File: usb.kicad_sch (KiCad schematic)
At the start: 10 parts, among them J7 USB_C_Receptacle_USB2.0, U28 USBLC6-4SC6

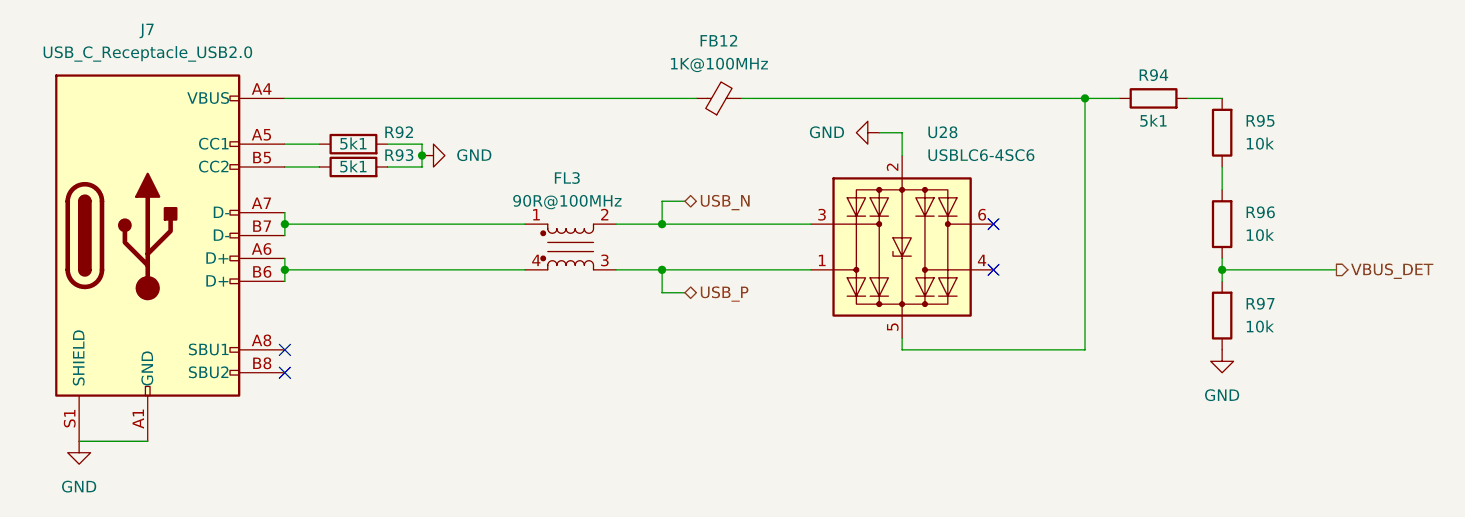
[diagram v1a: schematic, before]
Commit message: pcb: Finish Layout for rev0_3 - Assign MFR_PN for all Components - schematics changes:   - drivestage: Add Switch to optionally enable Modulation Signal Termination   -             Add alternate Precision Power Resistor   -             Modify the RC network values at TIA LPF Output   - MCU: Add Redundant 2.54mm pitch Programming Header   - thermostat: Duplicate the power filter network for alternate Temperature ADC
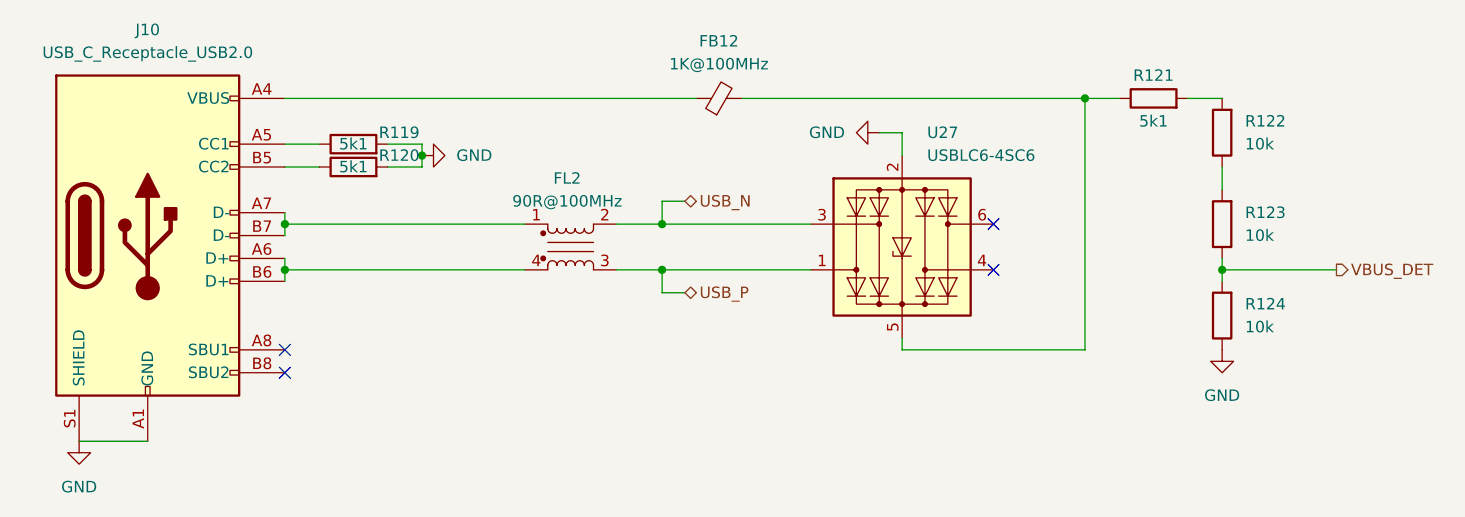
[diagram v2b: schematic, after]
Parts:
- renumbered FL3 to FL2, J7 to J10, R92 to R119, R93 to R120, R94 to R121, R95 to R122, R96 to R123, R97 to R124, U28 to U27
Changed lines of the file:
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@@
     (title "Kirdy")
     (date "2022-07-03")
-    (rev "r0.1")
+    (rev "r0.3")
     (company "M-Labs")
-    (comment 1 "Alex Wong Tat Hang")
+    (comment 1 "Linus Woo Chun Kit")
   )
   (junction (at 143.51 101.6) (diameter 0) (color 0 0 0 0)
@@
   (symbol (lib_id "power:GND") (at 247.65 115.57 0) (unit 1)
     (in_bom yes) (on_board yes) (dnp no) (fields_autoplaced)
-    (property "Reference" "#PWR0155" (at 247.65 121.92 0)
+    (property "Reference" "#PWR0184" (at 247.65 121.92 0)
       (effects (font (size 1.27 1.27)) hide)
     )
@@
       (project "kirdy"
         (path "/88da1dd8-9274-4b55-84fb-90006c9b6e8f/70187dee-b8b1-417f-999f-47b1dfda0f58"
-          (reference "#PWR0155") (unit 1)
+          (reference "#PWR0184") (unit 1)
         )
       )
@@
   (symbol (lib_id "power:GND") (at 158.75 93.98 90) (unit 1)
     (in_bom yes) (on_board yes) (dnp no) (fields_autoplaced)
-    (property "Reference" "#PWR0153" (at 165.1 93.98 0)
+    (property "Reference" "#PWR0182" (at 165.1 93.98 0)
       (effects (font (size 1.27 1.27)) hide)
     )
@@
       (project "kirdy"
         (path "/88da1dd8-9274-4b55-84fb-90006c9b6e8f/70187dee-b8b1-417f-999f-47b1dfda0f58"
-          (reference "#PWR0153") (unit 1)
+          (reference "#PWR0182") (unit 1)
         )
       )
@@
   (symbol (lib_id "power:GND") (at 209.55 91.44 270) (unit 1)
     (in_bom yes) (on_board yes) (dnp no) (fields_autoplaced)
-    (property "Reference" "#PWR0154" (at 203.2 91.44 0)
+    (property "Reference" "#PWR0183" (at 203.2 91.44 0)
       (effects (font (size 1.27 1.27)) hide)
     )
@@
       (project "kirdy"
         (path "/88da1dd8-9274-4b55-84fb-90006c9b6e8f/70187dee-b8b1-417f-999f-47b1dfda0f58"
-          (reference "#PWR0154") (unit 1)
+          (reference "#PWR0183") (unit 1)
         )
       )
@@
   (symbol (lib_id "Connector:USB_C_Receptacle_USB2.0") (at 128.27 102.87 0) (unit 1)
     (in_bom yes) (on_board yes) (dnp no) (fields_autoplaced)
-    (property "Reference" "J7" (at 128.27 80.01 0)
+    (property "Reference" "J10" (at 128.27 80.01 0)
       (effects (font (size 1.27 1.27)))
     )
@@
       (project "kirdy"
         (path "/88da1dd8-9274-4b55-84fb-90006c9b6e8f/70187dee-b8b1-417f-999f-47b1dfda0f58"
-          (reference "J7") (unit 1)
+          (reference "J10") (unit 1)
         )
       )
@@
   (symbol (lib_id "Device:R") (at 151.13 92.71 90) (unit 1)
     (in_bom yes) (on_board yes) (dnp no)
-    (property "Reference" "R92" (at 156.21 91.44 90)
+    (property "Reference" "R119" (at 156.21 91.44 90)
       (effects (font (size 1.27 1.27)))
     )
@@
       (project "kirdy"
         (path "/88da1dd8-9274-4b55-84fb-90006c9b6e8f/70187dee-b8b1-417f-999f-47b1dfda0f58"
-          (reference "R92") (unit 1)
+          (reference "R119") (unit 1)
         )
       )
@@
   (symbol (lib_id "Device:R") (at 247.65 111.76 180) (unit 1)
     (in_bom yes) (on_board yes) (dnp no) (fields_autoplaced)
-    (property "Reference" "R97" (at 250.19 110.4899 0)
+    (property "Reference" "R124" (at 250.19 110.4899 0)
       (effects (font (size 1.27 1.27)) (justify right))
     )
@@
       (project "kirdy"
         (path "/88da1dd8-9274-4b55-84fb-90006c9b6e8f/70187dee-b8b1-417f-999f-47b1dfda0f58"
-          (reference "R97") (unit 1)
+          (reference "R124") (unit 1)
         )
       )
@@
   (symbol (lib_id "Power_Protection:USBLC6-4SC6") (at 212.09 104.14 0) (mirror x) (unit 1)
     (in_bom yes) (on_board yes) (dnp no) (fields_autoplaced)
-    (property "Reference" "U28" (at 214.8587 91.44 0)
+    (property "Reference" "U27" (at 214.8587 91.44 0)
       (effects (font (size 1.27 1.27)) (justify left))
     )
@@
       (project "kirdy"
         (path "/88da1dd8-9274-4b55-84fb-90006c9b6e8f/70187dee-b8b1-417f-999f-47b1dfda0f58"
-          (reference "U28") (unit 1)
+          (reference "U27") (unit 1)
         )
       )
@@
   (symbol (lib_id "Device:R") (at 151.13 95.25 90) (unit 1)
     (in_bom yes) (on_board yes) (dnp no)
-    (property "Reference" "R93" (at 156.21 93.98 90)
+    (property "Reference" "R120" (at 156.21 93.98 90)
       (effects (font (size 1.27 1.27)))
     )
@@
       (project "kirdy"
         (path "/88da1dd8-9274-4b55-84fb-90006c9b6e8f/70187dee-b8b1-417f-999f-47b1dfda0f58"
-          (reference "R93") (unit 1)
+          (reference "R120") (unit 1)
         )
       )
@@
   (symbol (lib_id "Device:R") (at 240.03 87.63 90) (unit 1)
     (in_bom yes) (on_board yes) (dnp no)
-    (property "Reference" "R94" (at 240.03 85.09 90)
+    (property "Reference" "R121" (at 240.03 85.09 90)
       (effects (font (size 1.27 1.27)))
     )
@@
       (project "kirdy"
         (path "/88da1dd8-9274-4b55-84fb-90006c9b6e8f/70187dee-b8b1-417f-999f-47b1dfda0f58"
-          (reference "R94") (unit 1)
+          (reference "R121") (unit 1)
         )
       )
@@
   (symbol (lib_id "Device:R") (at 247.65 101.6 180) (unit 1)
     (in_bom yes) (on_board yes) (dnp no) (fields_autoplaced)
-    (property "Reference" "R96" (at 250.19 100.3299 0)
+    (property "Reference" "R123" (at 250.19 100.3299 0)
       (effects (font (size 1.27 1.27)) (justify right))
     )
@@
       (project "kirdy"
         (path "/88da1dd8-9274-4b55-84fb-90006c9b6e8f/70187dee-b8b1-417f-999f-47b1dfda0f58"
-          (reference "R96") (unit 1)
+          (reference "R123") (unit 1)
         )
       )
@@
   (symbol (lib_id "Device:R") (at 247.65 91.44 180) (unit 1)
     (in_bom yes) (on_board yes) (dnp no) (fields_autoplaced)
-    (property "Reference" "R95" (at 250.19 90.1699 0)
+    (property "Reference" "R122" (at 250.19 90.1699 0)
       (effects (font (size 1.27 1.27)) (justify right))
     )
@@
       (project "kirdy"
         (path "/88da1dd8-9274-4b55-84fb-90006c9b6e8f/70187dee-b8b1-417f-999f-47b1dfda0f58"
-          (reference "R95") (unit 1)
+          (reference "R122") (unit 1)
         )
       )
@@
   (symbol (lib_id "kirdy:Filter_EMI_LL_1423") (at 175.26 104.14 0) (unit 1)
     (in_bom yes) (on_board yes) (dnp no)
-    (property "Reference" "FL3" (at 174.879 96.52 0)
+    (property "Reference" "FL2" (at 174.879 96.52 0)
       (effects (font (size 1.27 1.27)))
     )
@@
       (project "kirdy"
         (path "/88da1dd8-9274-4b55-84fb-90006c9b6e8f/70187dee-b8b1-417f-999f-47b1dfda0f58"
-          (reference "FL3") (unit 1)
+          (reference "FL2") (unit 1)
         )
       )
@@
   (symbol (lib_id "power:GND") (at 120.65 125.73 0) (unit 1)
     (in_bom yes) (on_board yes) (dnp no) (fields_autoplaced)
-    (property "Reference" "#PWR0152" (at 120.65 132.08 0)
+    (property "Reference" "#PWR0181" (at 120.65 132.08 0)
       (effects (font (size 1.27 1.27)) hide)
     )
@@
       (project "kirdy"
         (path "/88da1dd8-9274-4b55-84fb-90006c9b6e8f/70187dee-b8b1-417f-999f-47b1dfda0f58"
-          (reference "#PWR0152") (unit 1)
-        )
-      )
+          (reference "#PWR0181") (unit 1)
+        )
+      )

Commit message: sch: Update Title Block Info - rev0.3 -> rev0_3 - Correct the title of each schematics - Update the modified time
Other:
- company: M-Labs -> M-Labs Limited
- title: Kirdy -> USB
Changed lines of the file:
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@@
   (paper "A3")
   (title_block
-    (title "Kirdy")
-    (date "2022-07-03")
-    (rev "r0.3")
-    (company "M-Labs")
+    (title "USB")
+    (date "2023-11-09")
+    (rev "r0_3")
+    (company "M-Labs Limited")
     (comment 1 "Linus Woo Chun Kit")
   )

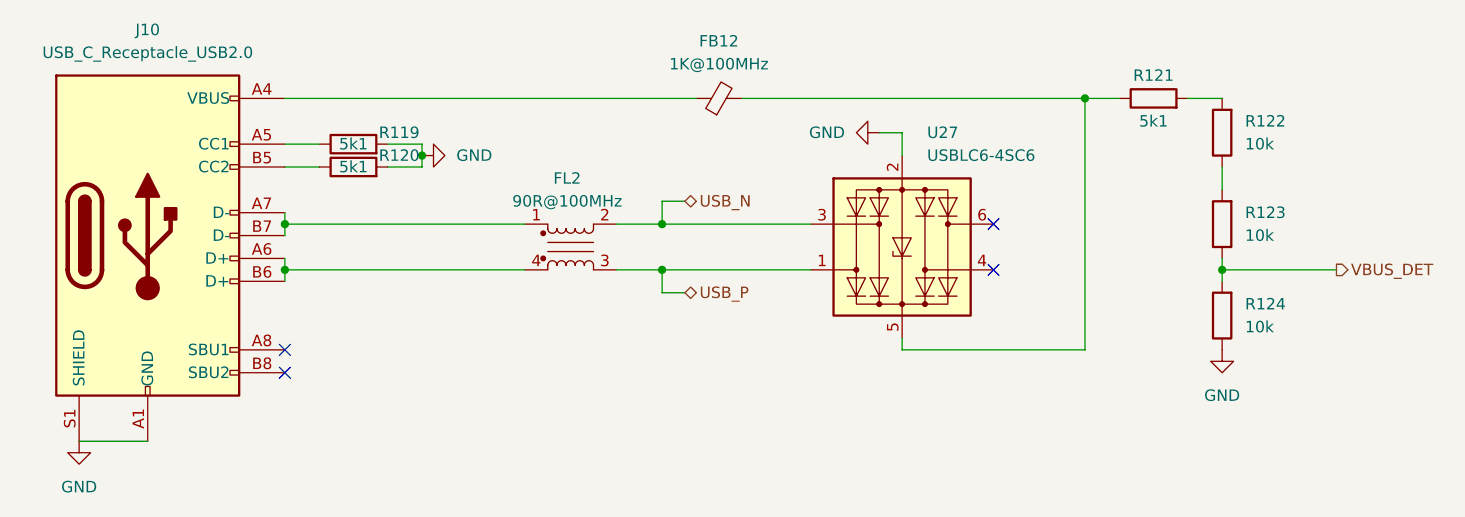
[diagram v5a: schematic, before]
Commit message: Reassign Reference Designators for all Symbols
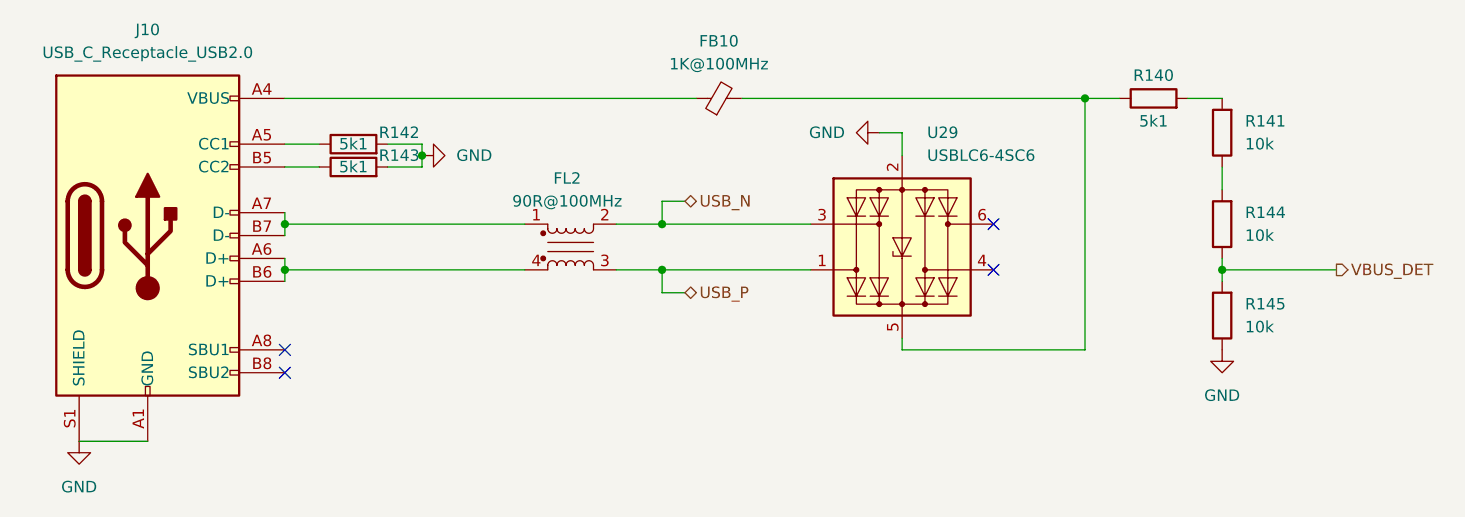
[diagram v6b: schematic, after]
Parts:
- renumbered FB12 to FB10, R121 to R140, R122 to R141, R119 to R142, R120 to R143, R123 to R144, R124 to R145, U27 to U29
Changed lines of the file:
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@@
   (symbol (lib_id "power:GND") (at 247.65 115.57 0) (unit 1)
     (in_bom yes) (on_board yes) (dnp no) (fields_autoplaced)
-    (property "Reference" "#PWR0185" (at 247.65 121.92 0)
+    (property "Reference" "#PWR0233" (at 247.65 121.92 0)
       (effects (font (size 1.27 1.27)) hide)
     )
@@
       (project "kirdy"
         (path "/88da1dd8-9274-4b55-84fb-90006c9b6e8f/70187dee-b8b1-417f-999f-47b1dfda0f58"
-          (reference "#PWR0185") (unit 1)
+          (reference "#PWR0233") (unit 1)
         )
       )
@@
   (symbol (lib_id "power:GND") (at 158.75 93.98 90) (unit 1)
     (in_bom yes) (on_board yes) (dnp no) (fields_autoplaced)
-    (property "Reference" "#PWR0183" (at 165.1 93.98 0)
+    (property "Reference" "#PWR0232" (at 165.1 93.98 0)
       (effects (font (size 1.27 1.27)) hide)
     )
@@
       (project "kirdy"
         (path "/88da1dd8-9274-4b55-84fb-90006c9b6e8f/70187dee-b8b1-417f-999f-47b1dfda0f58"
-          (reference "#PWR0183") (unit 1)
+          (reference "#PWR0232") (unit 1)
         )
       )
@@
   (symbol (lib_id "power:GND") (at 209.55 91.44 270) (unit 1)
     (in_bom yes) (on_board yes) (dnp no) (fields_autoplaced)
-    (property "Reference" "#PWR0184" (at 203.2 91.44 0)
+    (property "Reference" "#PWR0231" (at 203.2 91.44 0)
       (effects (font (size 1.27 1.27)) hide)
     )
@@
       (project "kirdy"
         (path "/88da1dd8-9274-4b55-84fb-90006c9b6e8f/70187dee-b8b1-417f-999f-47b1dfda0f58"
-          (reference "#PWR0184") (unit 1)
+          (reference "#PWR0231") (unit 1)
         )
       )
@@
   (symbol (lib_id "Device:R") (at 151.13 92.71 90) (unit 1)
     (in_bom yes) (on_board yes) (dnp no)
-    (property "Reference" "R119" (at 156.21 91.44 90)
+    (property "Reference" "R142" (at 156.21 91.44 90)
       (effects (font (size 1.27 1.27)))
     )
@@
       (project "kirdy"
         (path "/88da1dd8-9274-4b55-84fb-90006c9b6e8f/70187dee-b8b1-417f-999f-47b1dfda0f58"
-          (reference "R119") (unit 1)
+          (reference "R142") (unit 1)
         )
       )
@@
   (symbol (lib_id "Device:R") (at 247.65 111.76 180) (unit 1)
     (in_bom yes) (on_board yes) (dnp no) (fields_autoplaced)
-    (property "Reference" "R124" (at 250.19 110.4899 0)
+    (property "Reference" "R145" (at 250.19 110.4899 0)
       (effects (font (size 1.27 1.27)) (justify right))
     )
@@
       (project "kirdy"
         (path "/88da1dd8-9274-4b55-84fb-90006c9b6e8f/70187dee-b8b1-417f-999f-47b1dfda0f58"
-          (reference "R124") (unit 1)
+          (reference "R145") (unit 1)
         )
       )
@@
   (symbol (lib_id "Power_Protection:USBLC6-4SC6") (at 212.09 104.14 0) (mirror x) (unit 1)
     (in_bom yes) (on_board yes) (dnp no) (fields_autoplaced)
-    (property "Reference" "U27" (at 214.8587 91.44 0)
+    (property "Reference" "U29" (at 214.8587 91.44 0)
       (effects (font (size 1.27 1.27)) (justify left))
     )
@@
       (project "kirdy"
         (path "/88da1dd8-9274-4b55-84fb-90006c9b6e8f/70187dee-b8b1-417f-999f-47b1dfda0f58"
-          (reference "U27") (unit 1)
+          (reference "U29") (unit 1)
         )
       )
@@
   (symbol (lib_id "Device:FerriteBead_Small") (at 191.77 87.63 90) (unit 1)
     (in_bom yes) (on_board yes) (dnp no) (fields_autoplaced)
-    (property "Reference" "FB12" (at 191.7319 81.28 90)
+    (property "Reference" "FB10" (at 191.7319 81.28 90)
       (effects (font (size 1.27 1.27)))
     )
@@
       (project "kirdy"
         (path "/88da1dd8-9274-4b55-84fb-90006c9b6e8f/70187dee-b8b1-417f-999f-47b1dfda0f58"
-          (reference "FB12") (unit 1)
+          (reference "FB10") (unit 1)
         )
       )
@@
   (symbol (lib_id "Device:R") (at 151.13 95.25 90) (unit 1)
     (in_bom yes) (on_board yes) (dnp no)
-    (property "Reference" "R120" (at 156.21 93.98 90)
+    (property "Reference" "R143" (at 156.21 93.98 90)
       (effects (font (size 1.27 1.27)))
     )
@@
       (project "kirdy"
         (path "/88da1dd8-9274-4b55-84fb-90006c9b6e8f/70187dee-b8b1-417f-999f-47b1dfda0f58"
-          (reference "R120") (unit 1)
+          (reference "R143") (unit 1)
         )
       )
@@
   (symbol (lib_id "Device:R") (at 240.03 87.63 90) (unit 1)
     (in_bom yes) (on_board yes) (dnp no)
-    (property "Reference" "R121" (at 240.03 85.09 90)
+    (property "Reference" "R140" (at 240.03 85.09 90)
       (effects (font (size 1.27 1.27)))
     )
@@
       (project "kirdy"
         (path "/88da1dd8-9274-4b55-84fb-90006c9b6e8f/70187dee-b8b1-417f-999f-47b1dfda0f58"
-          (reference "R121") (unit 1)
+          (reference "R140") (unit 1)
         )
       )
@@
   (symbol (lib_id "Device:R") (at 247.65 101.6 180) (unit 1)
     (in_bom yes) (on_board yes) (dnp no) (fields_autoplaced)
-    (property "Reference" "R123" (at 250.19 100.3299 0)
+    (property "Reference" "R144" (at 250.19 100.3299 0)
       (effects (font (size 1.27 1.27)) (justify right))
     )
@@
       (project "kirdy"
         (path "/88da1dd8-9274-4b55-84fb-90006c9b6e8f/70187dee-b8b1-417f-999f-47b1dfda0f58"
-          (reference "R123") (unit 1)
+          (reference "R144") (unit 1)
         )
       )
@@
   (symbol (lib_id "Device:R") (at 247.65 91.44 180) (unit 1)
     (in_bom yes) (on_board yes) (dnp no) (fields_autoplaced)
-    (property "Reference" "R122" (at 250.19 90.1699 0)
+    (property "Reference" "R141" (at 250.19 90.1699 0)
       (effects (font (size 1.27 1.27)) (justify right))
     )
@@
       (project "kirdy"
         (path "/88da1dd8-9274-4b55-84fb-90006c9b6e8f/70187dee-b8b1-417f-999f-47b1dfda0f58"
-          (reference "R122") (unit 1)
+          (reference "R141") (unit 1)
         )
       )
@@
   (symbol (lib_id "power:GND") (at 120.65 125.73 0) (unit 1)
     (in_bom yes) (on_board yes) (dnp no) (fields_autoplaced)
-    (property "Reference" "#PWR0182" (at 120.65 132.08 0)
+    (property "Reference" "#PWR0234" (at 120.65 132.08 0)
       (effects (font (size 1.27 1.27)) hide)
     )
@@
       (project "kirdy"
         (path "/88da1dd8-9274-4b55-84fb-90006c9b6e8f/70187dee-b8b1-417f-999f-47b1dfda0f58"
-          (reference "#PWR0182") (unit 1)
-        )
-      )
+          (reference "#PWR0234") (unit 1)
+        )
+      )
